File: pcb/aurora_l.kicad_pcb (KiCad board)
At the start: 2 copper layers, 145.1 x 107.7 mm, 94 parts

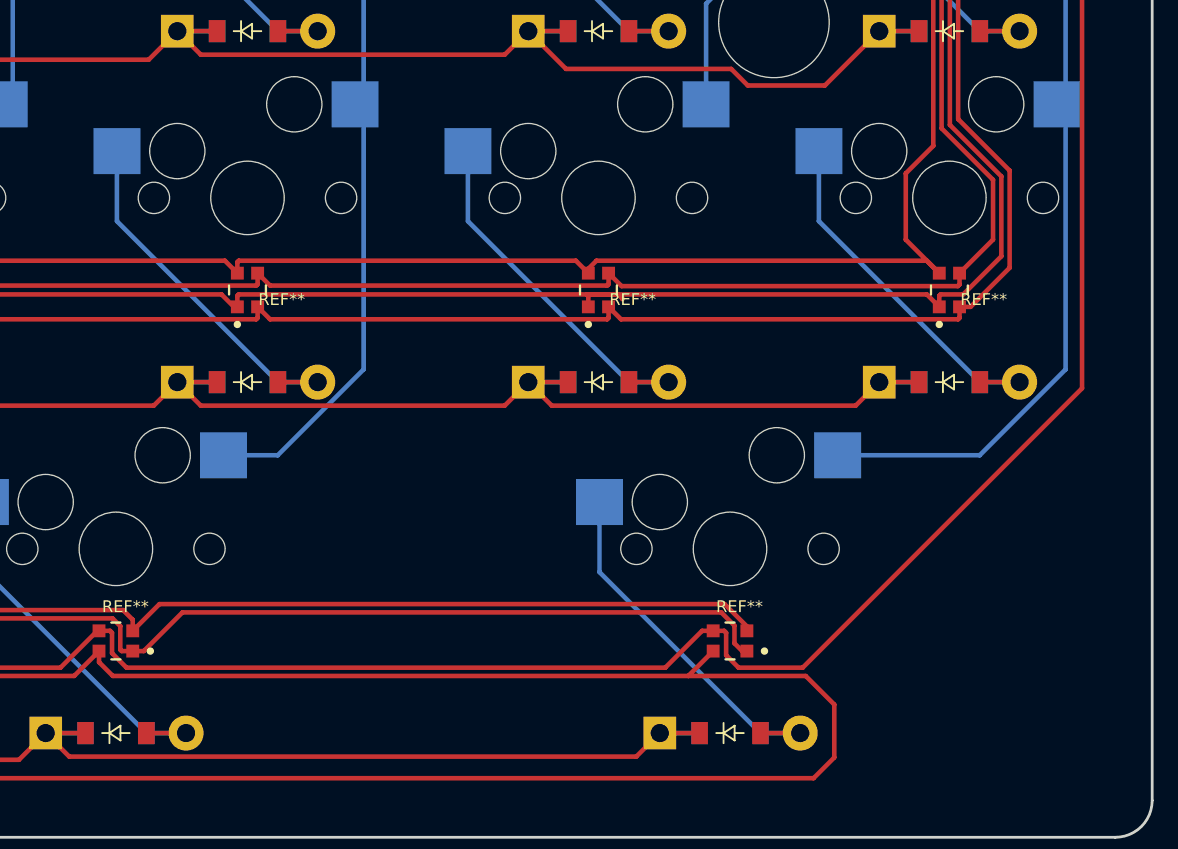
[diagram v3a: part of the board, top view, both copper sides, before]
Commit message: Add stab holes to PCBs
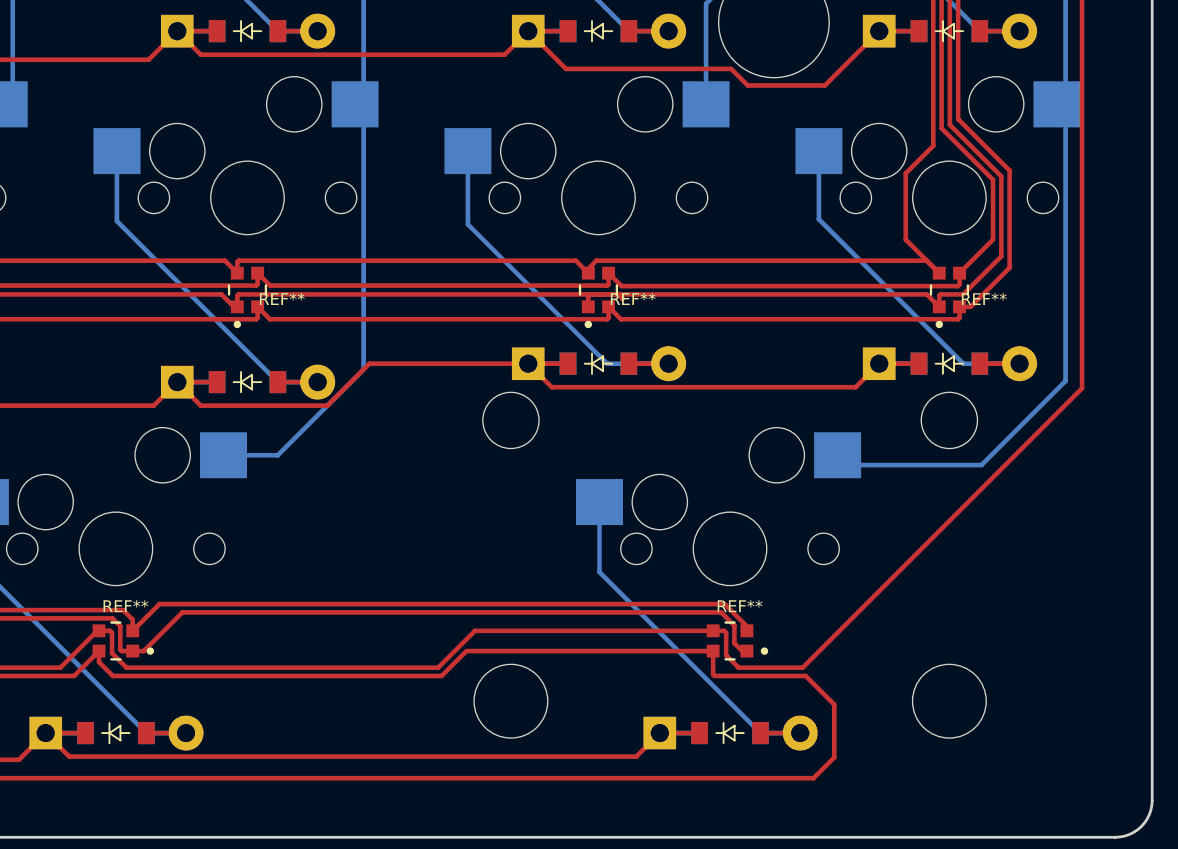
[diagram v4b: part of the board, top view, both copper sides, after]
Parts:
- added REF**: SW_Cherry_MX_2.25u_PCB, Button_Switch_Keyboard:SW_Cherry_MX_2.25u_PCB, F.Cu at (185.9, 114.0)
- moved D17 1.00 mm to (176.2, 109.0)
- moved D21 1.00 mm to (195.2, 109.0)
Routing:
- net P017: track 229.6 -> 230.4 mm

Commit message: Minor adjustment to left pcb
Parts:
- turned JST1 to 180 degrees
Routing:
- net BAT: track 14.8 -> 27.6 mm
- net RAW: track 88.8 -> 92.0 mm
- net GND: track 862.9 -> 863.5 mm
